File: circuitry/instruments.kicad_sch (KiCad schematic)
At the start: 34 parts, among them M1 105ZDY08, M2 12025, M3 9733, SW1 6A Momentary, SW2 6A SPDT, SW3 6A SPDT, SW4 6A Momentary SPDT

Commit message: chore: Organise & formate
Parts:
- S2: Friendly Name Temp & Pressure -> Atmospheric Sensor
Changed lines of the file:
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@@
 			)
 		)
-		(property "Friendly Name" "Temp & Pressure"
+		(property "Friendly Name" "Atmospheric Sensor"
 			(at 149.86 49.022 0)
 			(show_name no)

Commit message: feat: Add VESC config settings in README
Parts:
- BT1, BT2: Friendly Name VRLA Battery -> VRLA AGM Battery
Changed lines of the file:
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@@
 			)
 		)
-		(property "Friendly Name" "VRLA Battery"
+		(property "Friendly Name" "VRLA AGM Battery"
 			(at 273.304 37.592 90)
 			(show_name no)
@@
 			)
 		)
-		(property "Friendly Name" "VRLA Battery"
+		(property "Friendly Name" "VRLA AGM Battery"
 			(at 272.796 20.574 90)
 			(show_name no)

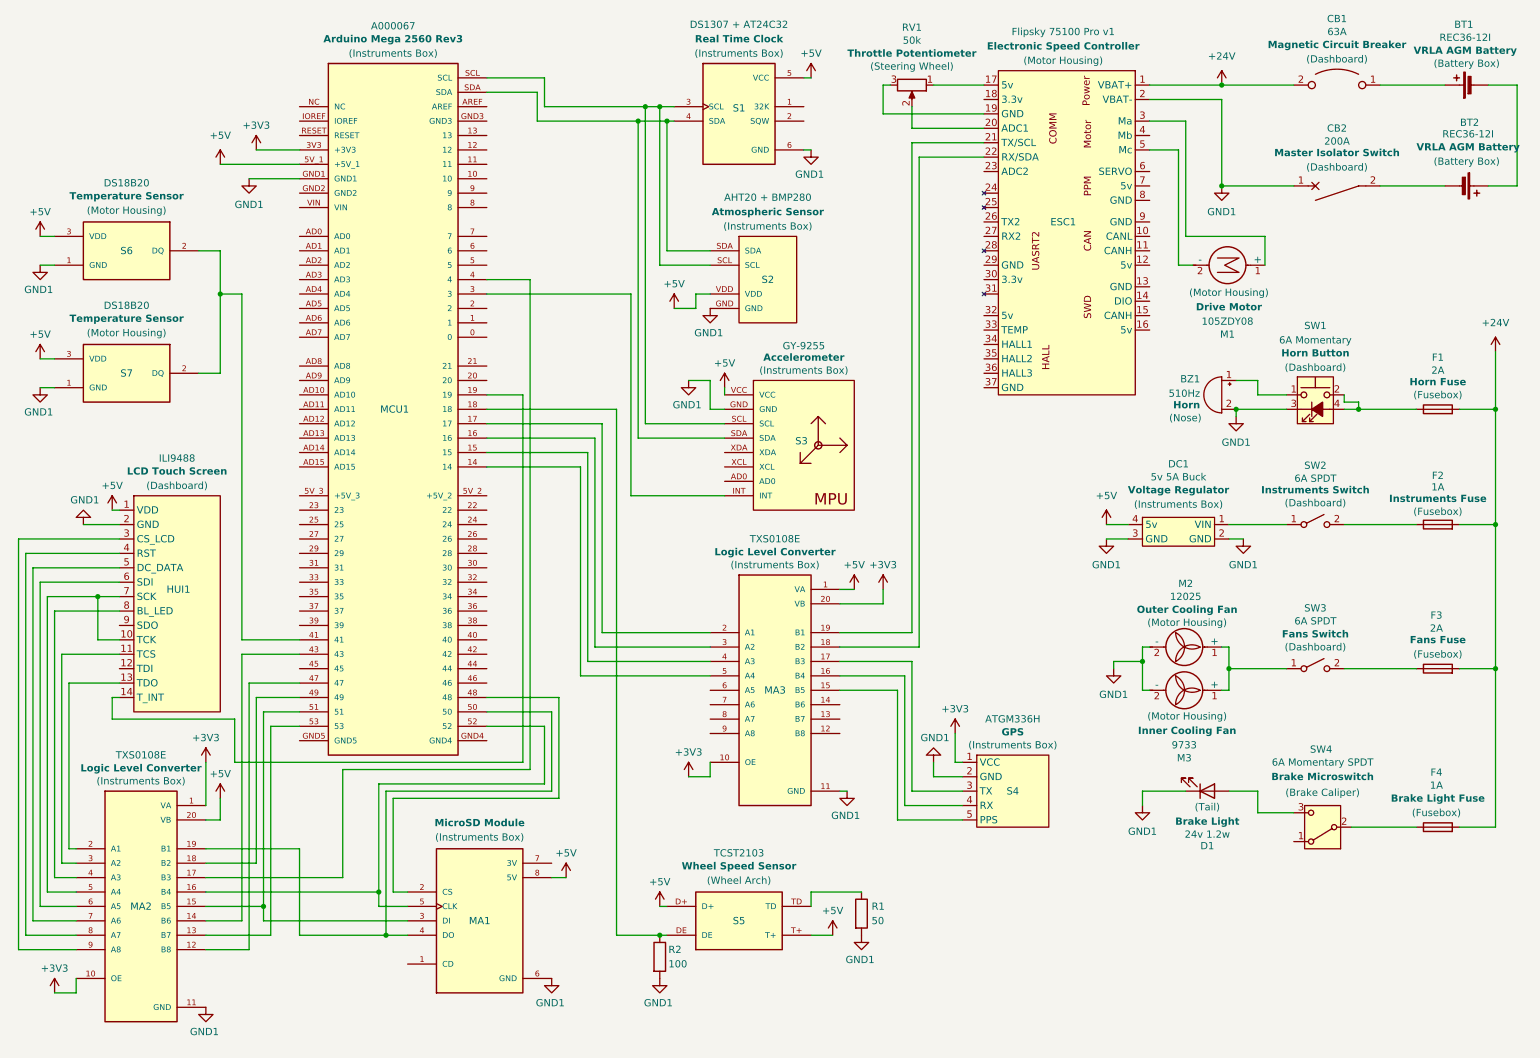
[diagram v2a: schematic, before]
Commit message: feat: Add connectors to circuit diagram
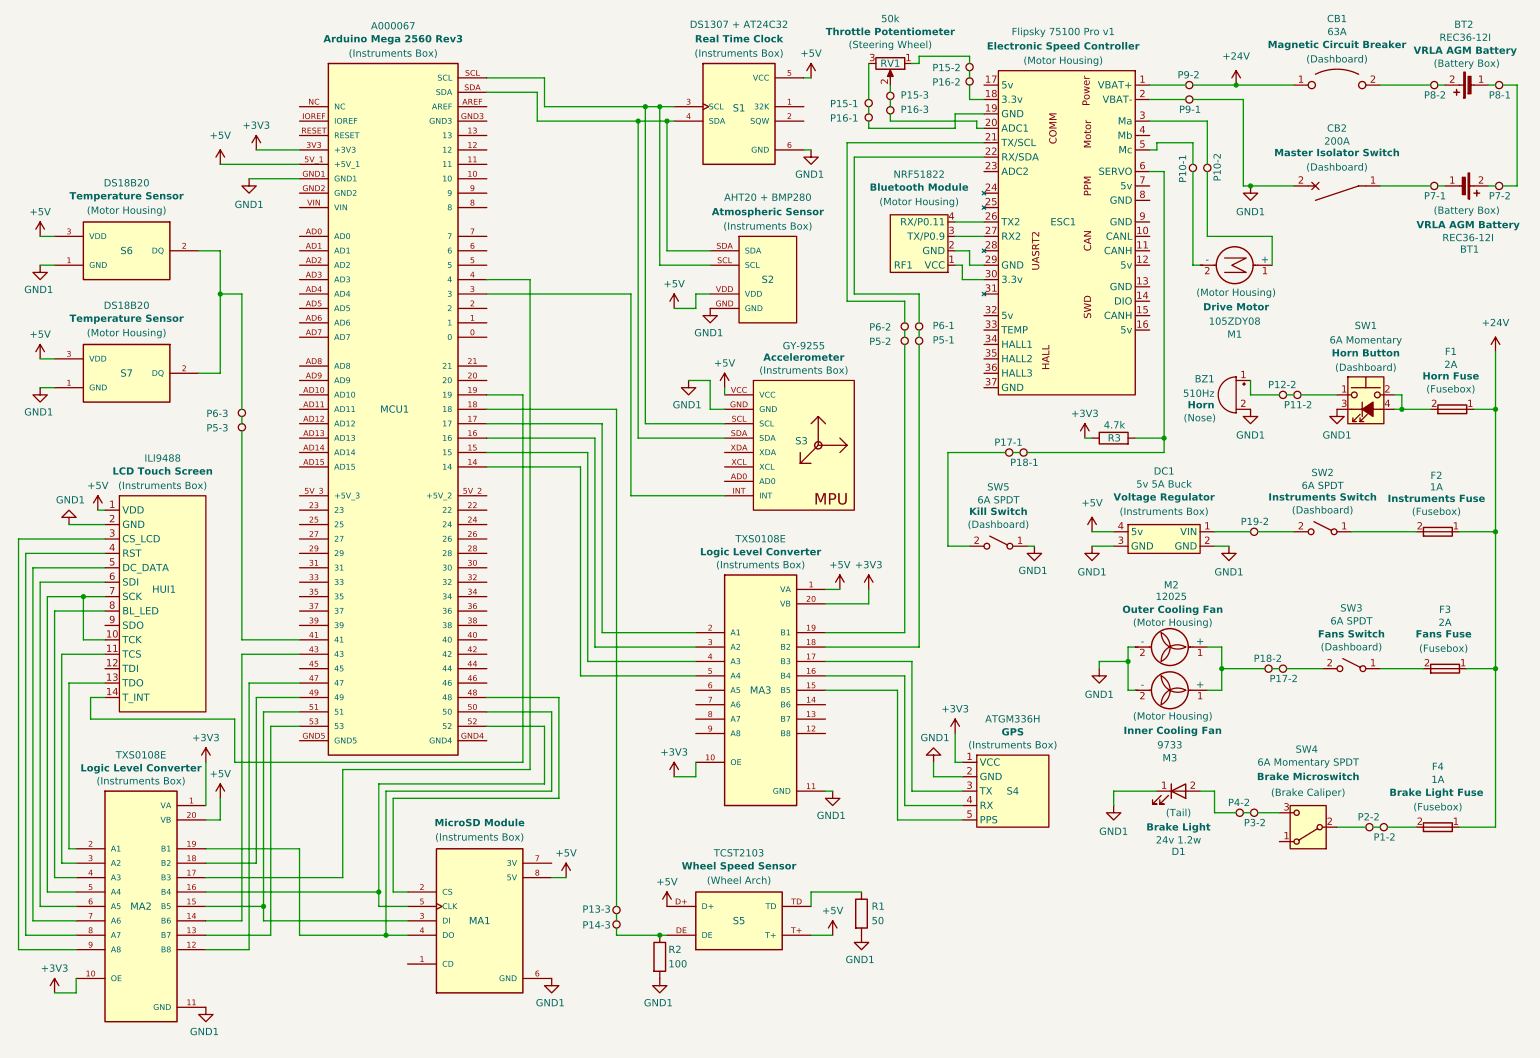
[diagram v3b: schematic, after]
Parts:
- added J38: P9-1, symbol Connector:TestPoint
- added J39: P9-2, symbol Connector:TestPoint
- added J40: P7-1, symbol Connector:TestPoint
- added J41: P7-2, symbol Connector:TestPoint
- added J42: P8-2, symbol Connector:TestPoint
- added J43: P8-1, symbol Connector:TestPoint
- added J49: P10-1, symbol Connector:TestPoint
- added J50: P10-2, symbol Connector:TestPoint
- added J53: P1-2, symbol Connector:TestPoint
- added J54: P2-2, symbol Connector:TestPoint
- added J55: P3-2, symbol Connector:TestPoint
- added J56: P4-2, symbol Connector:TestPoint
- added J57: P17-2, symbol Connector:TestPoint
- added J58: P18-2, symbol Connector:TestPoint
- added J59: P12-2, symbol Connector:TestPoint
- added J60: P11-2, symbol Connector:TestPoint
- added J63: P14-3, symbol Connector:TestPoint
- added J64: P13-3, symbol Connector:TestPoint
- added J72: P16-2, symbol Connector:TestPoint
- added J73: P15-2, symbol Connector:TestPoint
- added J76: P16-1, symbol Connector:TestPoint
- added J77: P15-1, symbol Connector:TestPoint
- added J78: P16-3, symbol Connector:TestPoint
- added J79: P15-3, symbol Connector:TestPoint
- added J81: P19-2, symbol Connector:TestPoint
- added J82: P17-1, symbol Connector:TestPoint
- added J83: P18-1, symbol Connector:TestPoint
- added J88: P5-1, symbol Connector:TestPoint
- added J89: P6-1, symbol Connector:TestPoint
- added J90: P5-2, symbol Connector:TestPoint
- added J91: P6-2, symbol Connector:TestPoint
- added J92: P6-3, symbol Connector:TestPoint
- added J93: P5-3, symbol Connector:TestPoint
- added R3: 4.7k, symbol Device:R
- added RF1: NRF51822, symbol Custom:NRF51822
- added SW5: 6A SPDT, symbol Switch:SW_SPST
- HUI1: Location (Dashboard) -> (Instruments Box)
- renumbered BT2 to BT1, BT1 to BT2
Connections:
- net +24V: now also CB1.1, F1.1, F2.1, F3.1, F4.1, J39.2; no longer CB1.2, ESC1.1 (VBAT+), F1.2, F2.2, F3.2, F4.2
- net +3V3: now also R3.1
- net GND1: now also CB2.2, J38.1, SW5.1 (A); no longer CB2.1, ESC1.2 (VBAT-)
- net at R2.1, S5.DE: now also J63.1; no longer MCU1.18
- net at SW3.2 (B): now also J57.1; no longer F3.1
- net at M1.1 (+): now also J50.2; no longer ESC1.3 (Ma)
- net at M1.2 (-): now also J49.1; no longer ESC1.5 (Mc)
- net at M2.1 (+), M3.1 (+): now also J58.1; no longer SW3.1 (A)
- net at SW4.2 (B): now also J54.1; no longer F4.1
- net at SW4.3 (C): now also J55.1; no longer D1.2 (A)
- net at BT2.1 (-): now also J43.2; no longer CB1.1
- net at BZ1.1 (+): now also J59.1; no longer SW1.1
- net at BT2.2 (+): now also J42.1; no longer BT1.1 (+)
- net at BT1.2 (+): now also J41.2; no longer CB2.2
- net at DC1.1 (VIN): now also J81.2; no longer SW2.1 (A)
- net at SW1.2, SW1.4 (A): now also F1.2; no longer F1.1
- net at RV1.1: now also J73.1; no longer ESC1.17 (5v)
- net at ESC1.18 (3.3v): now also J72.1
- net at RV1.3: now also J77.1; no longer ESC1.19 (GND)
- net at ESC1.20 (ADC1): now also J78.1; no longer RV1.2
- net at ESC1.21 (TX/SCL): now also J91.1; no longer MA3.19 (B1)
- net at MA3.18 (B2): now also J88.1; no longer ESC1.22 (RX/SDA)
- net at ESC1.26 (TX2): now also RF1.4 (RX/P0.11)
- net at ESC1.27 (RX2): now also RF1.3 (TX/P0.9)
- net at ESC1.29 (GND): now also RF1.2 (GND)
- net at ESC1.30 (3.3v): now also RF1.1 (VCC)
- net at ESC1.6 (SERVO): now also J83.1, R3.2
- net at S6.2 (DQ), S7.2 (DQ): now also J92.1; no longer MCU1.41
- net at SW2.2 (B): now also J81.1; no longer F2.1
- new net: J59.2, J60.2
- new net: J76.2, J77.2
- new net: F3.2, SW3.1 (A)
- new net: J82.1, SW5.2 (B)
- new net: J93.1, MCU1.41
- new net: J92.2, J93.2
- new net: ESC1.3 (Ma), J50.1
- new net: ESC1.1 (VBAT+), J39.1
- new net: CB1.2, J42.2
- new net: J64.1, MCU1.18
- new net: J63.2, J64.2
- new net: F4.2, J53.1
- new net: J53.2, J54.2
- new net: J41.1, J43.1
- new net: ESC1.5 (Mc), J49.2
- new net: J57.2, J58.2
- new net: J72.2, J73.2
- new net: BT1.1 (-), J40.1
- new net: J78.2, J79.2
- new net: CB2.1, J40.2
- new net: J88.2, J89.2
- new net: J60.1, SW1.1
- new net: ESC1.19 (GND), J76.1
- new net: ESC1.2 (VBAT-), J38.2
- new net: ESC1.22 (RX/SDA), J89.1
- new net: J82.2, J83.2
- new net: J79.1, RV1.2
- new net: D1.2 (A), J56.1
- new net: J90.1, MA3.19 (B1)
- new net: J90.2, J91.2
- new net: J55.2, J56.2
- new net: F2.2, SW2.1 (A)
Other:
- moved on the sheet: BZ1, DC1, HUI1, M1, M2, M3, MA3, RV1, SW1, SW2, SW3, SW4

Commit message: feat: Major circuit revision & refactor
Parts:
- removed BT1, BT2: REC36-12I, symbol Device:Battery_Cell
- removed BZ1: 510Hz, symbol Device:Buzzer
- removed CB1: 63A, symbol Device:CircuitBreaker_1P_US
- removed CB2: 200A, symbol Device:CircuitBreaker_1P
- removed D1: 24v 1.2w, symbol Device:LED
- removed DC1: 5v 5A Buck, symbol Custom:DC-DC
- removed ESC1: Flipsky 75100 Pro v1, symbol Custom:Flipsky_75100
- removed F1, F3: 2A, symbol Device:Fuse
- removed F2, F4: 1A, symbol Device:Fuse
- removed HUI1: ILI9488, symbol Custom:ILI9488_Display
- removed J38: P9-1, symbol Connector:TestPoint
- removed J39: P9-2, symbol Connector:TestPoint
- removed J40: P7-1, symbol Connector:TestPoint
- removed J41: P7-2, symbol Connector:TestPoint
- removed J42: P8-2, symbol Connector:TestPoint
- removed J43: P8-1, symbol Connector:TestPoint
- removed J49: P10-1, symbol Connector:TestPoint
- removed J50: P10-2, symbol Connector:TestPoint
- removed J53: P1-2, symbol Connector:TestPoint
- removed J54: P2-2, symbol Connector:TestPoint
- removed J55: P3-2, symbol Connector:TestPoint
- removed J56: P4-2, symbol Connector:TestPoint
- removed J57: P17-2, symbol Connector:TestPoint
- removed J58: P18-2, symbol Connector:TestPoint
- removed J59: P12-2, symbol Connector:TestPoint
- removed J60: P11-2, symbol Connector:TestPoint
- removed J63: P14-3, symbol Connector:TestPoint
- removed J64: P13-3, symbol Connector:TestPoint
- removed J72: P16-2, symbol Connector:TestPoint
- removed J73: P15-2, symbol Connector:TestPoint
- removed J76: P16-1, symbol Connector:TestPoint
- removed J77: P15-1, symbol Connector:TestPoint
- removed J78: P16-3, symbol Connector:TestPoint
- removed J79: P15-3, symbol Connector:TestPoint
- removed J81: P19-2, symbol Connector:TestPoint
- removed J82: P17-1, symbol Connector:TestPoint
- removed J83: P18-1, symbol Connector:TestPoint
- removed J88: P5-1, symbol Connector:TestPoint
- removed J89: P6-1, symbol Connector:TestPoint
- removed J90: P5-2, symbol Connector:TestPoint
- removed J91: P6-2, symbol Connector:TestPoint
- removed J92: P6-3, symbol Connector:TestPoint
- removed J93: P5-3, symbol Connector:TestPoint
- removed M1: 105ZDY08, symbol Motor:Motor_DC
- removed M2: 12025, symbol Motor:Fan
- removed M3: 9733, symbol Motor:Fan
- removed MA1: (no value), 254:MODULE_254, symbol Micro SD Module:254
- removed MA2, MA3: TXS0108E, ZC323900:MODULE_ZC323900, symbol Logic Level Shifter:ZC323900
- removed MCU1: A000067, A000067:MODULE_A000067, symbol Arduino Mega:A000067
- removed R1: 50, symbol Device:R
- removed R2: 100, symbol Device:R
- removed R3: 4.7k, symbol Device:R
- removed RF1: NRF51822, symbol Custom:NRF51822
- removed RV1: 50k, symbol Device:R_Potentiometer
- removed S1: DS1307 + AT24C32, TC00500:MODULE_TC00500, symbol Real Time Clock:TC00500
- removed S2: AHT20 + BMP280, AHT20_BMP280:AHT20_BMP280, symbol Temperature & Pressure:AHT20_BMP280
- removed S3: GY-9255, symbol Accelerometer:GY-521
- removed S4: ATGM336H, symbol Custom:ATGM336H
- removed S5: TCST2103, TCST2103:TCST2103, symbol Beam Break Sensor:TCST2103
- removed S6, S7: DS18B20, DS18B20_:IC_DS18B20_, symbol Temperature 1 Wire:DS18B20_
- removed SW1: 6A Momentary, symbol Switch:SW_Push_LED
- removed SW2, SW3, SW5: 6A SPDT, symbol Switch:SW_SPST
- removed SW4: 6A Momentary SPDT, symbol Switch:SW_SPDT
- added BT3, BT4: REC36-12I, symbol Device:Battery_Cell
- added BZ2: 510Hz, symbol Device:Buzzer
- added CB3: 63A, symbol Device:CircuitBreaker_1P_US
- added CB4: 200A, symbol Device:CircuitBreaker_1P
- added D2: 24v 1.2w, symbol Device:LED
- added DC2: 5v 5A Buck, symbol Custom:DC-DC
- added ESC2: Flipsky 75100 Pro v1, symbol Custom:Flipsky_75100
- added F5, F6: 1A, symbol Device:Fuse
- added F7, F8: 2A, symbol Device:Fuse
- added HUI2: ILI9488, symbol Custom:ILI9488_Display
- added J100: P6-2, symbol Connector:TestPoint
- added J101: P5-2, symbol Connector:TestPoint
- added J102: P6-1, symbol Connector:TestPoint
- added J103: P5-1, symbol Connector:TestPoint
- added J104: P15-2, symbol Connector:TestPoint
- added J105: P16-2, symbol Connector:TestPoint
- added J106: P17-1, symbol Connector:TestPoint
- added J107: P18-1, symbol Connector:TestPoint
- added J108: P9-2, symbol Connector:TestPoint
- added J109: P9-1, symbol Connector:TestPoint
- added J110: P10-1, symbol Connector:TestPoint
- added J111: P10-2, symbol Connector:TestPoint
- added J112: P4-2, symbol Connector:TestPoint
- added J113: P19-2, symbol Connector:TestPoint
- added J114: P3-2, symbol Connector:TestPoint
- added J115: P18-2, symbol Connector:TestPoint
- added J116: P12-2, symbol Connector:TestPoint
- added J117: P17-2, symbol Connector:TestPoint
- added J118: P11-2, symbol Connector:TestPoint
- added J119: P2-2, symbol Connector:TestPoint
- added J120: P1-2, symbol Connector:TestPoint
- added J121: P8-2, symbol Connector:TestPoint
- added J122: P7-1, symbol Connector:TestPoint
- added J123: P8-1, symbol Connector:TestPoint
- added J124: P7-2, symbol Connector:TestPoint
- added J86: P13-3, symbol Connector:TestPoint
- added J87: P14-3, symbol Connector:TestPoint
- added J94: P6-3, symbol Connector:TestPoint
- added J95: P5-3, symbol Connector:TestPoint
- added J96: P15-1, symbol Connector:TestPoint
- added J97: P16-1, symbol Connector:TestPoint
- added J98: P15-3, symbol Connector:TestPoint
- added J99: P16-3, symbol Connector:TestPoint
- added M4: 12025, symbol Motor:Fan
- added M5: 9733, symbol Motor:Fan
- added M6: 105ZDY08, symbol Motor:Motor_DC
- added MA4, MA6: TXS0108E, ZC323900:MODULE_ZC323900, symbol Logic Level Shifter:ZC323900
- added MA5: (no value), 254:MODULE_254, symbol Micro SD Module:254
- added MCU2: A000067, A000067:MODULE_A000067, symbol Arduino Mega:A000067
- added R4: 100, symbol Device:R
- added R5: 50, symbol Device:R
- added R6: 4.7k, symbol Device:R
- added RF2: NRF51822, symbol Custom:NRF51822
- added RV2: 50k, symbol Device:R_Potentiometer
- added S10: DS1307 + AT24C32, TC00500:MODULE_TC00500, symbol Real Time Clock:TC00500
- added S11: TCST2103, TCST2103:TCST2103, symbol Beam Break Sensor:TCST2103
- added S12: AHT20 + BMP280, AHT20_BMP280:AHT20_BMP280, symbol Temperature & Pressure:AHT20_BMP280
- added S13: GY-9255, symbol Accelerometer:GY-521
- added S14: ATGM336H, symbol Custom:ATGM336H
- added S8, S9: DS18B20, DS18B20_:IC_DS18B20_, symbol Temperature 1 Wire:DS18B20_
- added SW10: 6A Momentary, symbol Switch:SW_Push_LED
- added SW6, SW8, SW9: 6A SPDT, symbol Switch:SW_SPST
- added SW7: 6A Momentary SPDT, symbol Switch:SW_SPDT
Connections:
- net +24V: now also CB3.1, F5.1, F6.1, F7.1, F8.1, J108.2
- net +3V3: now also MA4.1 (VA), MA4.10 (OE), MA6.10 (OE), MA6.20 (VB), MCU2.3V3 (+3V3), R6.1, S14.1 (VCC)
- net +5V: now also DC2.4 (5v), HUI2.1 (VDD), MA4.20 (VB), MA5.8 (5V), MA6.1 (VA), MCU2.5V_1 (+5V_1), S10.5 (VCC), S11.D+, S11.T+, S12.VDD, S13.VCC, S8.3 (VDD), S9.3 (VDD)
- net GND1: now also BZ2.2 (-), CB4.2, D2.1 (K), DC2.2 (GND), DC2.3 (GND), HUI2.2 (GND), J109.1, M4.2 (-), M5.2 (-), MA4.11 (GND), MA5.6 (GND), MA6.11 (GND), MCU2.GND1, R4.2, R5.2, S10.6 (GND), S12.GND, S13.GND, S14.2 (GND), S8.1 (GND), S9.1 (GND), SW10.3 (K), SW6.1 (A)
- new net: J87.1, R4.1, S11.DE
- new net: J94.1, S8.2 (DQ), S9.2 (DQ)
- new net: BT4.2 (+), J121.1
- new net: CB3.2, J121.2
- new net: J103.1, MA6.18 (B2)
- new net: J102.2, J103.2
- new net: MCU2.SCL, S10.3 (SCL), S12.SCL, S13.SCL
- new net: MCU2.SDA, S10.4 (SDA), S12.SDA, S13.SDA
- new net: J106.1, SW6.2 (B)
- new net: J106.2, J107.2
- new net: J123.1, J124.1
- new net: BT4.1 (-), J123.2
- new net: J111.2, M6.1 (+)
- new net: J110.1, M6.2 (-)
- new net: BZ2.1 (+), J116.1
- new net: J116.2, J118.2
- new net: F7.2, SW9.1 (A)
- new net: J86.2, J87.2
- new net: ESC2.6 (SERVO), J107.1, R6.2
- new net: BT3.2 (+), J124.2
- new net: D2.2 (A), J112.1
- new net: F6.2, J120.1
- new net: CB4.1, J122.2
- new net: J94.2, J95.2
- new net: J119.2, J120.2
- new net: J104.1, RV2.1
- new net: J104.2, J105.2
- new net: ESC2.19 (GND), J97.1
- new net: J96.2, J97.2
- new net: ESC2.22 (RX/SDA), J102.1
- new net: J86.1, MCU2.18
- new net: J118.1, SW10.1
- new net: J98.1, RV2.2
- new net: J96.1, RV2.3
- new net: MA5.2 (CS), MCU2.48
- new net: MA4.15 (B5), MA5.3 (DI), MCU2.51
- new net: MA4.19 (B1), MA5.4 (DO), MCU2.50
- new net: MA4.16 (B4), MA5.5 (CLK), MCU2.52
- new net: ESC2.1 (VBAT+), J108.1
- new net: ESC2.18 (3.3v), J105.1
- new net: ESC2.2 (VBAT-), J109.2
- new net: ESC2.20 (ADC1), J99.1
- new net: ESC2.21 (TX/SCL), J100.1
- new net: ESC2.26 (TX2), RF2.4 (RX/P0.11)
- new net: ESC2.27 (RX2), RF2.3 (TX/P0.9)
- new net: ESC2.29 (GND), RF2.2 (GND)
- new net: ESC2.3 (Ma), J111.1
- new net: ESC2.30 (3.3v), RF2.1 (VCC)
- new net: ESC2.5 (Mc), J110.2
- new net: J113.1, SW8.2 (B)
- new net: DC2.1 (VIN), J113.2
- new net: J114.1, SW7.3 (C)
- new net: J112.2, J114.2
- new net: J119.1, SW7.2 (B)
- new net: MA6.17 (B3), S14.3 (TX)
- new net: MA6.16 (B4), S14.4 (RX)
- new net: MA6.15 (B5), S14.5 (PPS)
- new net: J95.1, MCU2.41
- new net: F8.2, SW10.2, SW10.4 (A)
- new net: J98.2, J99.2
- new net: BT3.1 (-), J122.1
- new net: J115.1, M4.1 (+), M5.1 (+)
- new net: J115.2, J117.2
- new net: R5.1, S11.TD
- new net: F5.2, SW8.1 (A)
- new net: MA4.12 (B8), MCU2.47
- new net: MA4.13 (B7), MCU2.53
- new net: MA4.14 (B6), MCU2.43
- new net: MA4.17 (B3), MCU2.4
- new net: MA4.18 (B2), MCU2.49
- new net: HUI2.13 (TDO), MA4.2 (A1)
- new net: HUI2.11 (TCS), MA4.3 (A2)
- new net: HUI2.8 (BL_LED), MA4.4 (A3)
- new net: HUI2.10 (TCK), HUI2.7 (SCK), MA4.5 (A4)
- new net: HUI2.6 (SDI), MA4.6 (A5)
- new net: HUI2.5 (DC_DATA), MA4.7 (A6)
- new net: HUI2.4 (RST), MA4.8 (A7)
- new net: HUI2.3 (CS_LCD), MA4.9 (A8)
- new net: J117.1, SW9.2 (B)
- new net: J101.1, MA6.19 (B1)
- new net: MA6.2 (A1), MCU2.17
- new net: MA6.3 (A2), MCU2.16
- new net: MA6.4 (A3), MCU2.15
- new net: MA6.5 (A4), MCU2.14
- new net: J100.2, J101.2
- new net: MCU2.3, S13.INT
- new net: HUI2.14 (T_INT), MCU2.19
